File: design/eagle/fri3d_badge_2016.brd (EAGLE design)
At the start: 80 x 70 mm, 40 parts, among them K1 65100516121, Q1 MOSFET-NCHANNEL2N7002PW, U1 MCP73831

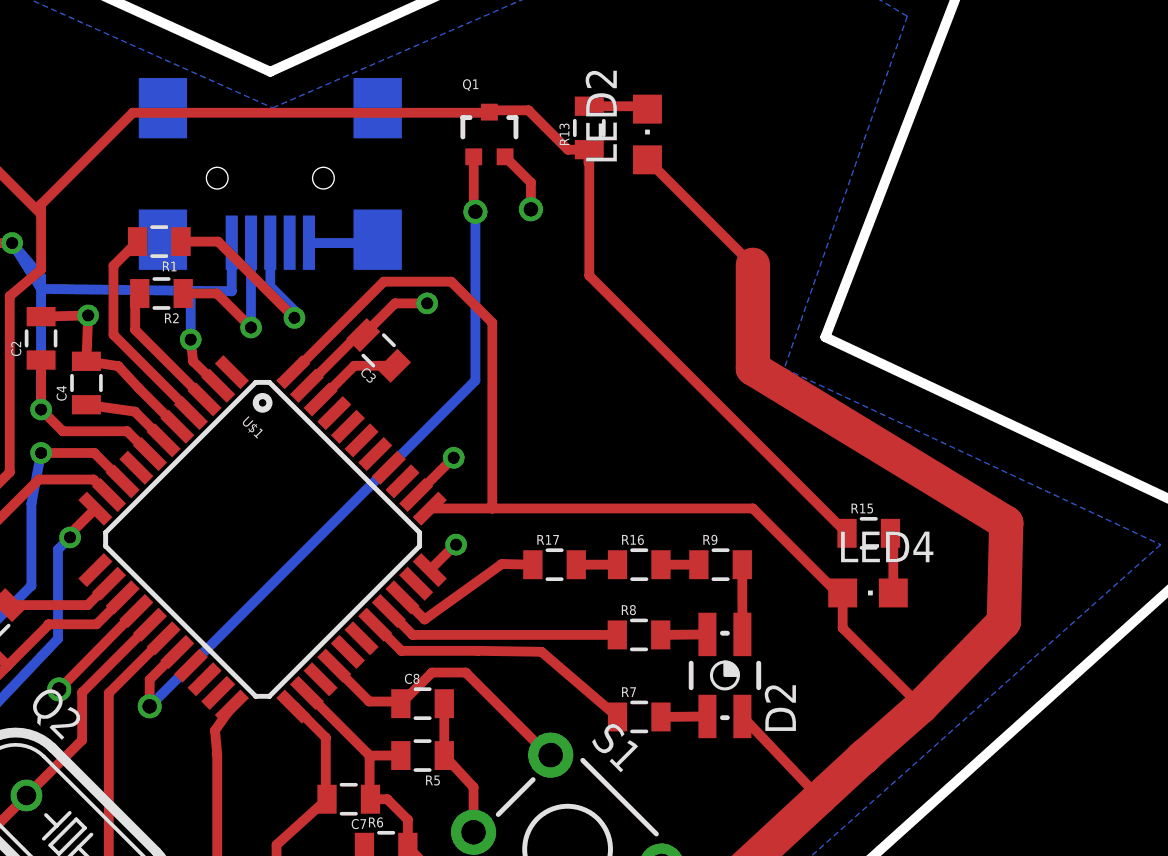
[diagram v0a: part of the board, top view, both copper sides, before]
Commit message: added header for Analog pins A0-5
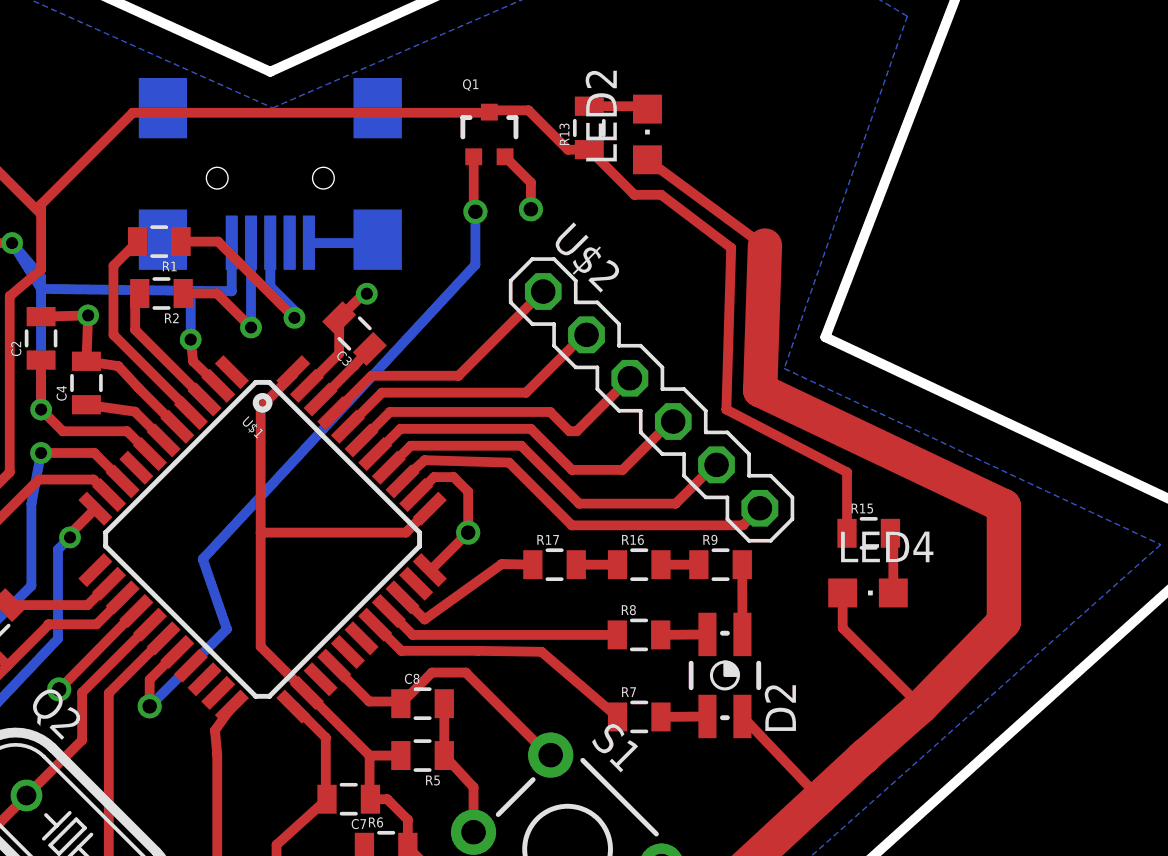
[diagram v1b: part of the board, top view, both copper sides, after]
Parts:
- added U$2: HEADER-06X1-MALE, GeekAmmo:06X1-PTH
- moved C3 1.22 mm to (43.5, 44.1)
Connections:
- new net A0: U$1.36, U$2.6
- new net A1: U$1.37, U$2.5
- new net A2: U$1.38, U$2.4
- new net A3: U$1.39, U$2.3
- new net A4: U$1.40, U$2.2
- new net A5: U$1.41, U$2.1
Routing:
- net A0: track 0.00 -> 16.5 mm
- net A1: track 0.00 -> 15.6 mm
- net A2: track 0.00 -> 14.3 mm
- net VCC: track 261.7 -> 248.6 mm
- net A3: track 0.00 -> 12.9 mm
- net A4: track 0.00 -> 11.5 mm
- net A5: track 0.00 -> 10.7 mm
- net GND: track 54.5 -> 55.9 mm, vias 9 -> 8
- net N$24: track 76.0 -> 77.4 mm
- net N$7: track 3.62 -> 2.93 mm

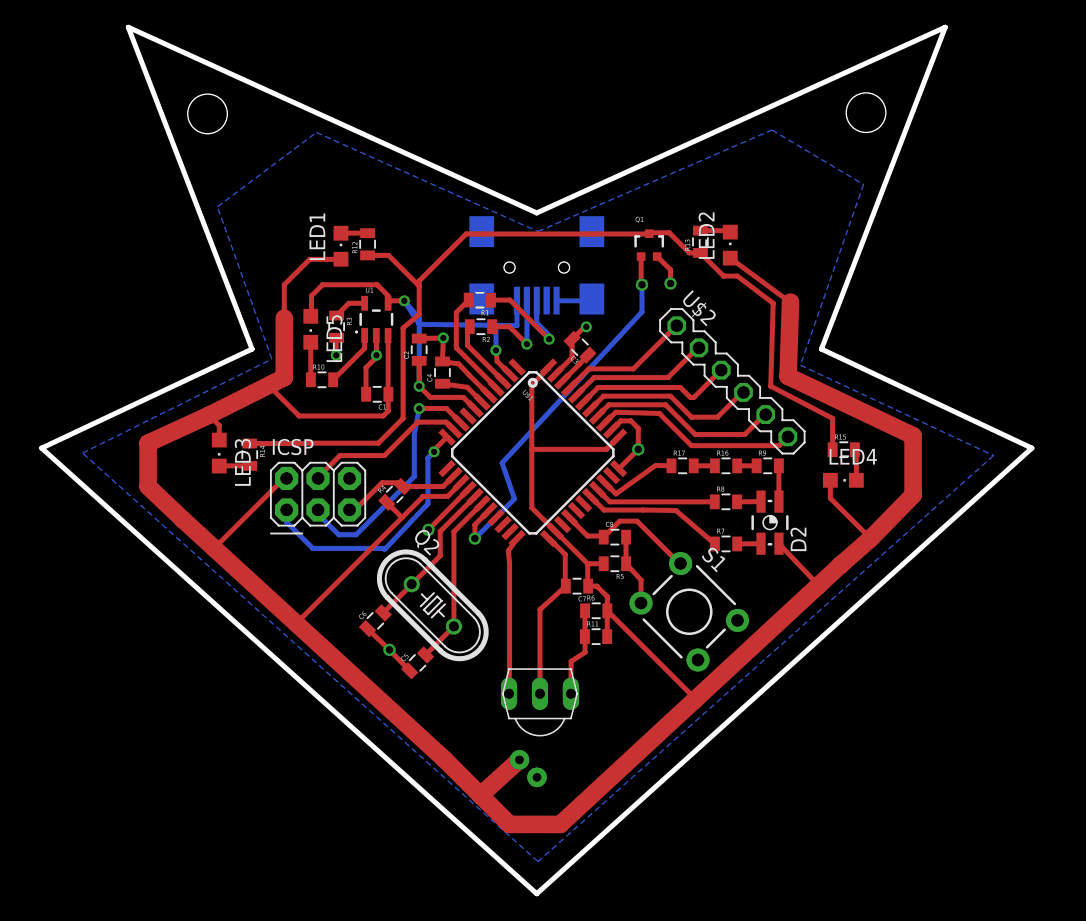
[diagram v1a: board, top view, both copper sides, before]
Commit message: fixed IR receiver and button Arduino pins
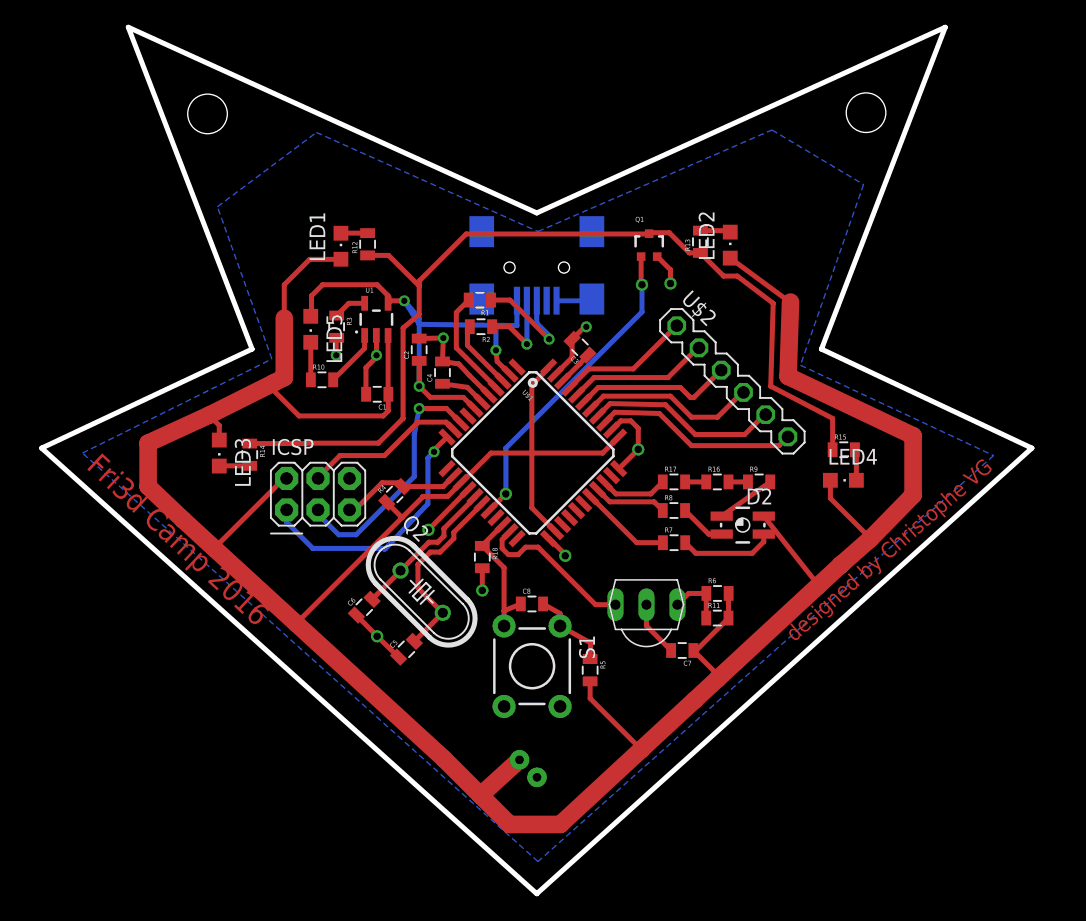
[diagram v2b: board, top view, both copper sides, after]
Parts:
- added R18: 10K, SparkFun-Passives:0805
- moved S1 13.4 mm to (39.6, 18.4), turned to 270 degrees
- moved U$3 11.2 mm to (48.9, 23.4)
- moved C7 9.96 mm to (51.8, 19.6)
- moved R11 9.91 mm to (54.6, 22.3)
- moved R6 9.90 mm to (54.6, 24.3)
- moved R5 8.83 mm to (44.3, 18.1), turned to 270 degrees
- moved C8 8.61 mm to (39.6, 23.4)
- moved R8 4.26 mm to (51.1, 31.0)
- moved R7 4.20 mm to (51.1, 28.4)
- moved D2 2.21 mm to (56.6, 29.8), turned to 90 degrees
- moved R17 1.48 mm to (51.1, 33.3)
- moved R16 1.48 mm to (54.6, 33.3)
- moved R9 1.48 mm to (58.0, 33.3)
- moved C5 1.42 mm to (29.5, 19.8)
- moved C6 1.42 mm to (26.1, 23.1)
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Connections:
- net BUTTON: now also R18.1, S1.3, U$1.20; no longer S1.1, U$1.26
- net GND: now also R18.2
- net IR_RX: now also U$1.21; no longer U$1.22
- net N$3: now also S1.1; no longer S1.3
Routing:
- net N$19: track 1.93 -> 7.71 mm
- net IR_TX: track 31.5 -> 25.7 mm
- net GND: track 55.9 -> 50.2 mm, vias 8 -> 10
- net RGB_BLUE: track 11.5 -> 7.39 mm
- net RGB_GREEN: track 9.88 -> 5.97 mm
- net VCC: track 248.6 -> 252.0 mm
- net N$10: track 7.32 -> 4.71 mm
- net N$21: track 2.89 -> 4.80 mm
- net N$20: track 1.94 -> 3.75 mm
- net N$8: track 14.1 -> 15.5 mm
- net RGB_RED: track 6.52 -> 5.49 mm
- net N$3: track 5.80 -> 6.71 mm
- net BUTTON: track 11.6 -> 11.1 mm
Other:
- board text added: "Fri3d Camp 2016"
- board text added: "designed by Christophe VG"

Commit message: added switch and draft silkscreen
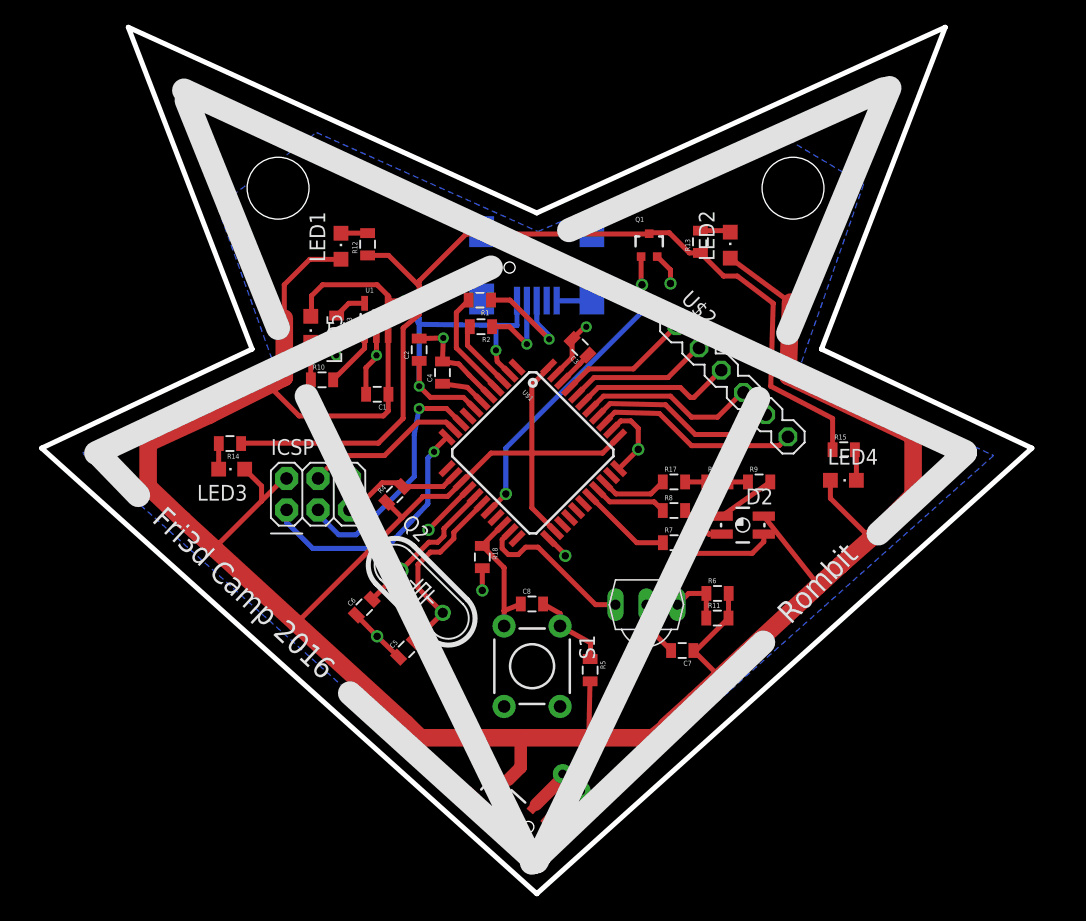
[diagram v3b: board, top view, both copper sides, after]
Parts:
- added S2: (no value), SparkFun-Electromechanical:SWITCH-SPST-SMD-A
- moved J3 3.67 mm to (43.2, 9.40), turned to 43 degrees
- moved R14 1.84 mm to (15.2, 36.4), turned to 180 degrees
- moved LED3 1.64 mm to (15.3, 34.3), turned to 90 degrees
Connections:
- new net N$17: J3.2, S2.2
- net VCC: now also S2.3; no longer J3.2
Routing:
- net VCC: track 252.0 -> 244.1 mm
- net N$17: track 0.00 -> 3.35 mm
- net N$24: track 77.4 -> 78.1 mm
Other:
- board text added: "Rombit"
- board text removed: "designed by Christophe VG"

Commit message: changed resistors on RGB LED to 220 (to test)
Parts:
- R16, R17, R7, R8, R9: value 22 -> 220
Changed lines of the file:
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@@
 <element name="R14" library="SparkFun-Passives" package="0805" value="220" x="15.21" y="36.37" rot="R180"/>
 <element name="R15" library="SparkFun-Passives" package="0805" value="220" x="64.8" y="35.87"/>
-<element name="R16" library="SparkFun-Passives" package="0805" value="22" x="54.59" y="33.27"/>
-<element name="R17" library="SparkFun-Passives" package="0805" value="22" x="51.08" y="33.27"/>
+<element name="R16" library="SparkFun-Passives" package="0805" value="220" x="54.59" y="33.27"/>
+<element name="R17" library="SparkFun-Passives" package="0805" value="220" x="51.08" y="33.27"/>
 <element name="R2" library="SparkFun-Passives" package="0805" value="22" x="35.49" y="45.81" rot="R180"/>
 <element name="R3" library="SparkFun-Passives" package="0805" value="10K" x="23.83" y="45.81" rot="R270"/>
@@
 <element name="R5" library="SparkFun-Passives" package="0805" value="220" x="44.31" y="18.06" rot="R270"/>
 <element name="R6" library="SparkFun-Passives" package="0805" value="220" x="54.6" y="24.26"/>
-<element name="R7" library="SparkFun-Passives" package="0805" value="22" x="51.09" y="28.36"/>
-<element name="R8" library="SparkFun-Passives" package="0805" value="22" x="51.08" y="30.96"/>
-<element name="R9" library="SparkFun-Passives" package="0805" value="22" x="57.96" y="33.27"/>
+<element name="R7" library="SparkFun-Passives" package="0805" value="220" x="51.09" y="28.36"/>
+<element name="R8" library="SparkFun-Passives" package="0805" value="220" x="51.08" y="30.96"/>
+<element name="R9" library="SparkFun-Passives" package="0805" value="220" x="57.96" y="33.27"/>
 <element name="S1" library="SparkFun-Electromechanical" package="TACTILE-PTH" value="SWITCH-MOMENTARY-2PTH" x="39.62" y="18.38" rot="R270">
 <attribute name="PROD_ID" value=" SWCH-08441" x="39.62" y="18.38" size="1.778" layer="27" rot="R270" display="off"/>

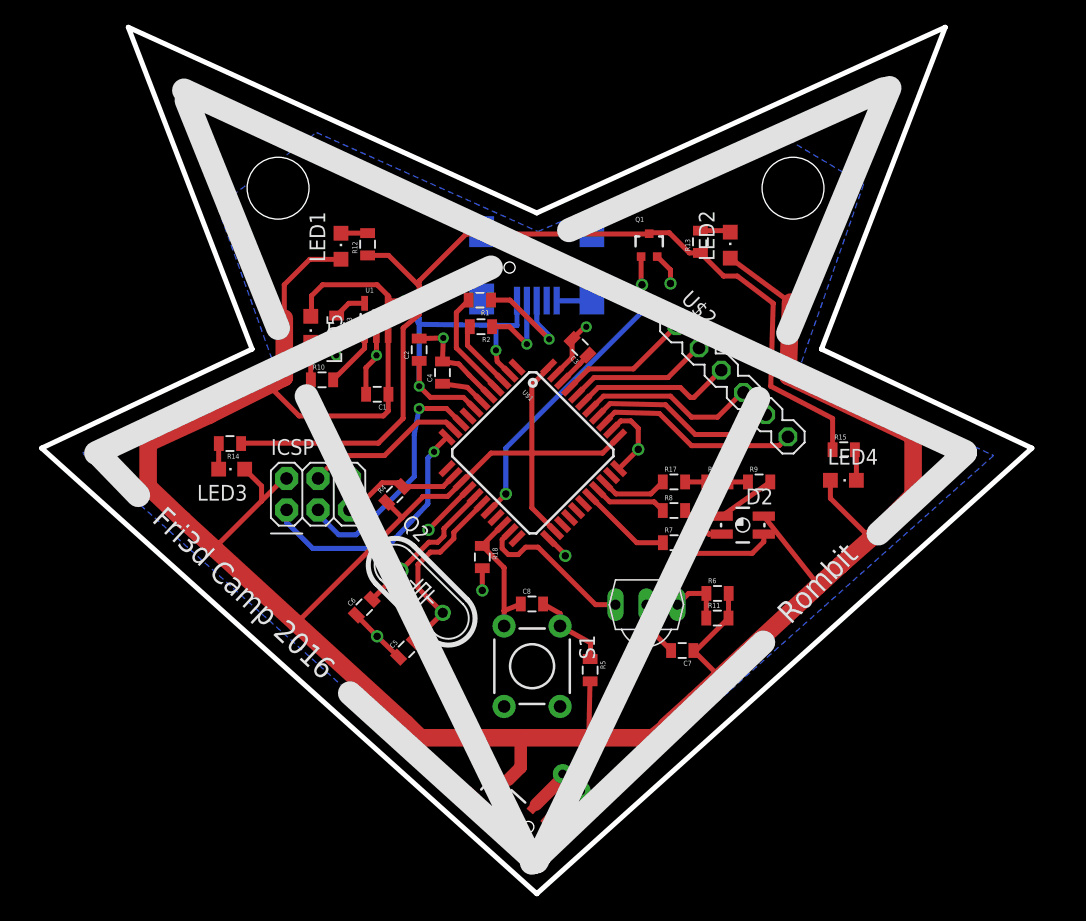
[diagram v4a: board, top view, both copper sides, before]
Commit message: fixed RGB LED footprint (+draft silk)
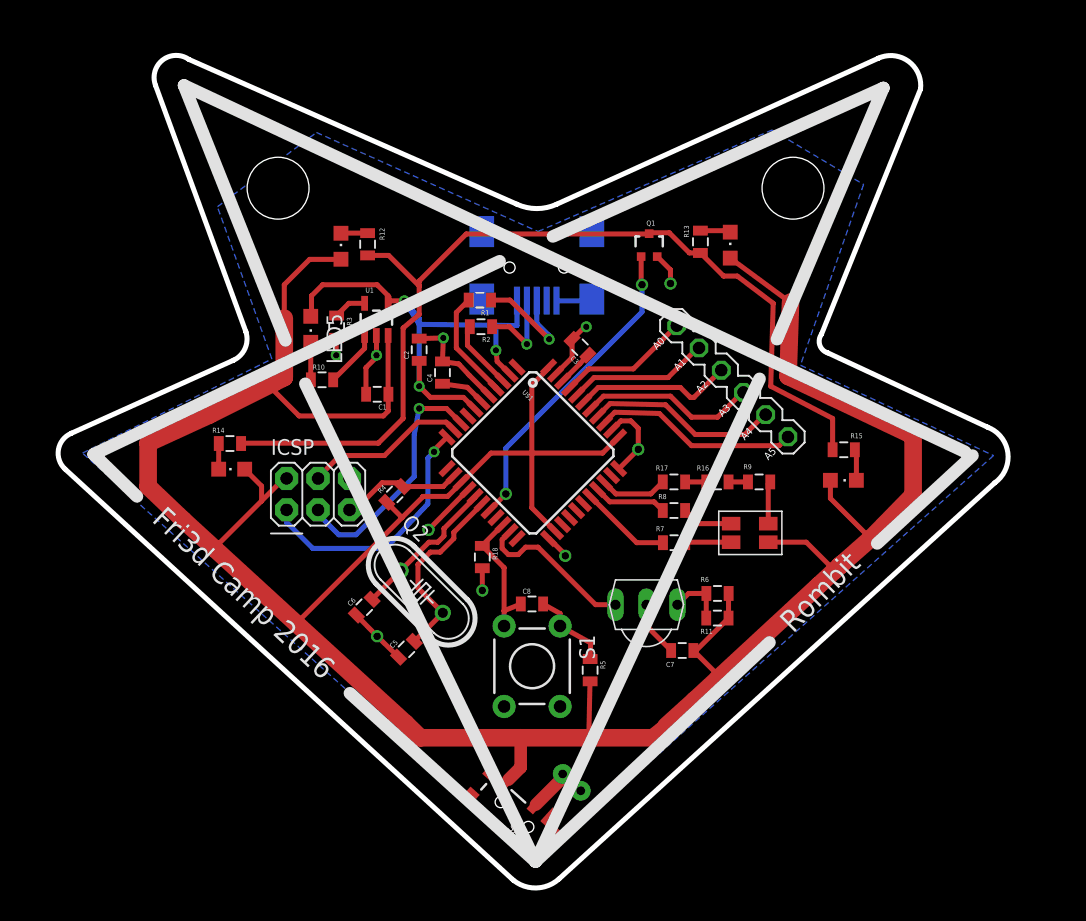
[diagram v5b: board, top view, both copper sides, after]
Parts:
- removed D2: (no value), SparkFun-LED:P-LCC-4-3
- added U$4: DRAGAN-PERSONAL_AVAGO-RGB-LED, Badge_EZR_V1:DRAGAN-PERSONAL_AVAGO-RGB-LED
- LED1: value (none) -> IR LED 1
- LED2: value (none) -> IR LED 2
- LED3: value (none) -> IR LED 3
- LED4: value (none) -> IR LED 4
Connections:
- removed net N$21: D2.1, R9.2
- new net N$18: R9.2, U$4.P$4
- net N$19: now also R8.2, U$4.P$3; no longer D2.3, R7.2
- net N$20: now also R7.2, U$4.P$2; no longer D2.2, R8.2
- net VCC: now also U$4.P$1; no longer D2.4
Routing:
- net N$21: track 4.80 -> 0.00 mm
- net N$19: track 7.71 -> 4.16 mm
- net N$18: track 0.00 -> 3.44 mm
- net VCC: track 244.1 -> 243.3 mm
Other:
- board size 80 x 70 mm -> 76.7 x 67.3 mm
- board text added: "A0"
- board text added: "A1"
- board text added: "A2"
- board text added: "A3"
- board text added: "A4"
- board text added: "A5"

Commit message: fixed USB connector (Mouser)
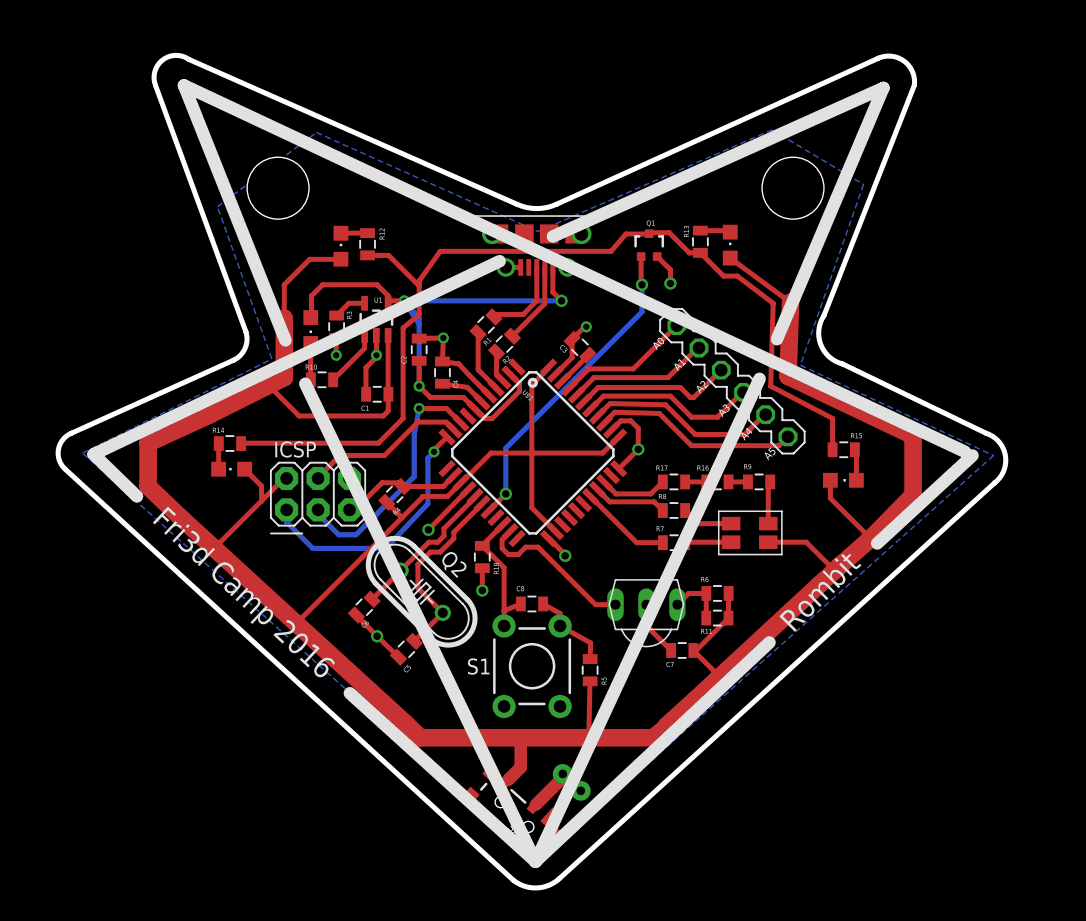
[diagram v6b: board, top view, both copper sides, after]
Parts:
- removed K1: 65100516121, Input-Output_Connectors_rev15d:65100516121
- added U$5: OCTA-CORE_MCIRO-USB2MOUSER, OCTA-EZR_v1:OCTA-CORE_MICRO-USB2
- LED5: value (none) -> LED
- moved R2 2.36 mm to (37.4, 44.4), turned to 225 degrees
- moved R1 2.06 mm to (35.9, 46.0), turned to 225 degrees
- moved LED5 0.10 mm to (21.7, 45.5)
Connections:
- net GND: now also U$5.P$10, U$5.P$11, U$5.P$12, U$5.P$13, U$5.P$5, U$5.P$6, U$5.P$7, U$5.P$8, U$5.P$9; no longer K1.5, K1.Z1, K1.Z2, K1.Z3, K1.Z4
- net N$1: now also U$5.P$2; no longer K1.2
- net N$2: now also U$5.P$3; no longer K1.3
- net USBVCC: now also U$5.P$1; no longer K1.1
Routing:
- net USBVCC: track 41.9 -> 49.8 mm
- net D+: track 8.91 -> 5.13 mm
- net D-: track 5.66 -> 2.58 mm
- net N$2: track 9.54 -> 6.70 mm, vias 1 -> 0
- net GND: track 50.2 -> 48.4 mm
- net N$1: track 6.91 -> 6.64 mm, vias 1 -> 0
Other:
- board size 76.7 x 67.3 mm -> 76.6 x 67.3 mm
